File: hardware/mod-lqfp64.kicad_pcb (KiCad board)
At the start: 2 copper layers, 25.1 x 14.5 mm, 12 parts, among them J1 Target, U1 STM32F405RGTx, Y1 8MHz

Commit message: Use Rezonit solder mask parameters
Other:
- rule pad_to_mask_clearance: 0 -> 0.05
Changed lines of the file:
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@@
     (pad_size 1.524 1.524)
     (pad_drill 0.762)
-    (pad_to_mask_clearance 0)
+    (pad_to_mask_clearance 0.05)
+    (solder_mask_min_width 0.15)
     (aux_axis_origin 0 0)
     (visible_elements FFFDFF7F)
@@
       (viasonmask false)
       (mode 1)
-      (useauxorigin false)
+      (useauxorigin true)
       (hpglpennumber 1)
       (hpglpenspeed 20)
@@
       (outputformat 1)
       (mirror false)
-      (drillshape 1)
+      (drillshape 0)
       (scaleselection 1)
-      (outputdirectory ""))
+      (outputdirectory "out64"))
   )
   (net 0 "")

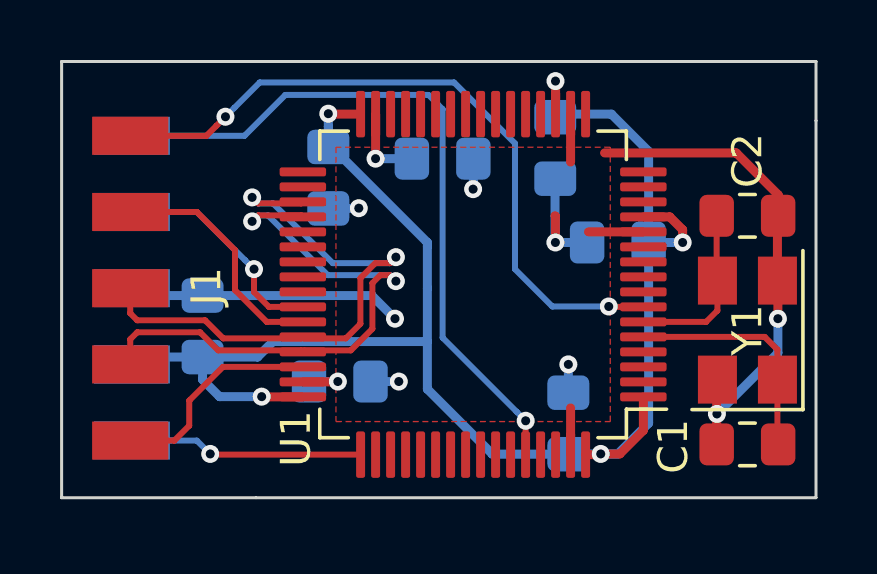
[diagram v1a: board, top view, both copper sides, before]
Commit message: Align boards to the 1mm grid
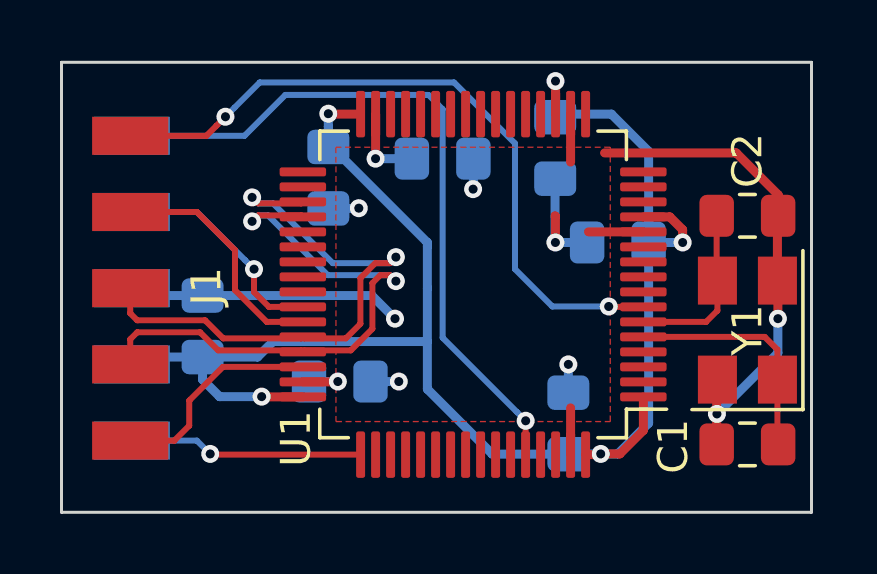
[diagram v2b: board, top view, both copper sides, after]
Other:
- board size 25.1 x 14.5 mm -> 25 x 15 mm
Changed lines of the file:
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@@
   (general
     (thickness 1.6)
-    (drawings 6)
+    (drawings 4)
     (tracks 199)
     (zones 0)
@@
     (pad_to_mask_clearance 0.05)
     (solder_mask_min_width 0.15)
-    (aux_axis_origin 0 0)
+    (aux_axis_origin 32 42)
     (visible_elements FFFDFF7F)
     (pcbplotparams
@@
     )
   )
-  (gr_line (start 32.004 41.9735) (end 32.004 56.515) (layer Edge.Cuts) (width 0.1))
-  (gr_line (start 57.15 41.9735) (end 57.15 43.942) (layer Edge.Cuts) (width 0.1))
-  (gr_line (start 32.004 41.9735) (end 57.15 41.9735) (layer Edge.Cuts) (width 0.1))
-  (gr_line (start 57.15 56.515) (end 57.15 43.942) (layer Edge.Cuts) (width 0.1))
-  (gr_line (start 38.481 56.515) (end 57.15 56.515) (layer Edge.Cuts) (width 0.1))
-  (gr_line (start 32.004 56.515) (end 38.481 56.515) (layer Edge.Cuts) (width 0.1))
+  (gr_line (start 32 42) (end 32 57) (layer Edge.Cuts) (width 0.1))
+  (gr_line (start 32 42) (end 57 42) (layer Edge.Cuts) (width 0.1))
+  (gr_line (start 57 57) (end 57 42) (layer Edge.Cuts) (width 0.1))
+  (gr_line (start 32 57) (end 57 57) (layer Edge.Cuts) (width 0.1))
   (segment (start 55.44 51.153) (end 51.395 51.153) (width 0.2) (layer F.Cu) (net 1))
   (segment (start 55.864 52.577) (end 55.864 51.577) (width 0.2) (layer F.Cu) (net 1))
